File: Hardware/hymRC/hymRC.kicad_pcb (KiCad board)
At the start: 2 copper layers, 97.8 x 97.8 mm, 206 parts, among them J1 Relay_0, J10 EXT_AUD_IN, J11 EXT_AUD_OUT, J2 Digital Sensor Connector, J3 Analog Sensor Connector, J4 TX RADIO, J5 RX RADIO, J6 Relay_1, J7 Relay_2, J8 Relay_3, J9 Relay_4, K1 Role, K2 Role, K3 Role, K4 Role, K5 Role, Q1 BC817, Q2 NPN, Q3 NPN, Q4 NPN, Q5 NPN, U1 KT8870, U10 OptoCoupler, U11 OptoCoupler, U12 OptoCoupler, U13 OptoCoupler, U14 OptoCoupler, U2 MCP23017_SP, U3 OptoCoupler, U4 OptoCoupler, U5 OptoCoupler, U6 TL084, U7 TL084, U8 LM7808_TO220, U9 L7805, Y1 3.5795M

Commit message: Audio section completed
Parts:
- C10, C11, C12, C14, C15, C16, C17, C18, C19, C20, C21, C22, C23, C24, C25, C26, C27, C28, C29, C30, C31, C32, C33, C34, C35, C36, C37, C40, C41, C42, C43, C8, C9, R25, R26, R27, R28, R29, R30, R33, R34, R35, R36, R37, R38, R39, R42, R43, R48, R49, R50, R51, R52, R53, R54, R55, R56, R57, R58, R59, R60, R62, R63, R64, R65, U6, U7: moved to B.Cu
- moved C15 284.2 mm to (244.3, 79.2), turned to 90 degrees
- moved C37 283.8 mm to (237.5, 124.5)
- moved C16 279.9 mm to (233.0, 85.7), turned to 90 degrees
- moved C30 271.4 mm to (234.6, 108.3)
- moved C42 270.7 mm to (229.1, 124.6), turned to 180 degrees
- moved C41 269.6 mm to (229.1, 126.9)
- moved C13 269.1 mm to (219.7, 76.7), turned to 180 degrees
- moved C33 268.6 mm to (241.8, 111.5), turned to 90 degrees
- moved C36 267.4 mm to (224.7, 123.3), turned to 180 degrees
- moved C35 263.1 mm to (224.7, 129.4)
- moved C32 261.8 mm to (238.6, 112.6), turned to 180 degrees
- moved C34 259.2 mm to (237.4, 126.9), turned to 180 degrees
- moved C26 254.7 mm to (228.1, 108.3)
- moved C12 250.4 mm to (226.1, 85.1), turned to 90 degrees
- moved C43 246.8 mm to (229.1, 68.8), turned to 90 degrees
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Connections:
- C40 pad 1: Net-(C40-Pad1) -> GND
- C40 pad 2: Net-(C40-Pad2) -> Aku_12V
- C41 pad 1: Net-(C41-Pad1) -> GND
- C41 pad 2: Net-(C41-Pad2) -> Aku_12V
- C42 pad 1: Net-(C41-Pad2) -> Aku_12V
- C42 pad 2: Net-(C41-Pad1) -> GND
- C43 pad 1: Net-(C40-Pad2) -> Aku_12V
- C43 pad 2: Net-(C40-Pad1) -> GND
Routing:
- net Net-(C13-Pad2): track 0.00 -> 44.2 mm, vias 0 -> 2
- net /VCC_2: track 0.00 -> 42.6 mm, vias 0 -> 5
- net Net-(C12-Pad1): track 0.00 -> 22.8 mm, vias 0 -> 1
- net Net-(R33-Pad2): track 0.00 -> 20.7 mm
- net Aku_12V: track 0.00 -> 20.5 mm
- net Net-(C15-Pad2): track 0.00 -> 19.2 mm, vias 0 -> 1
- net Net-(R63-Pad2): track 0.00 -> 14.1 mm
- net Net-(C16-Pad2): track 0.00 -> 14.0 mm
- net Net-(C26-Pad2): track 0.00 -> 13.9 mm
- net Net-(R24-Pad2): track 0.00 -> 12.1 mm
- net Net-(C20-Pad1): track 0.00 -> 11.7 mm, vias 0 -> 1
- net Net-(R28-Pad2): track 0.00 -> 10.8 mm
- net Net-(C10-Pad2): track 0.00 -> 10.4 mm
- net GND: track 0.00 -> 9.86 mm
- net Net-(C8-Pad2): track 0.00 -> 9.29 mm, vias 0 -> 1
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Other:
- net class orta added: clearance 0.2, trace_width 0.5, via_dia 1, via_drill 0.5

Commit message: all connected somehow
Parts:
- added ?: , , F.Cu at (117.2, 120.6)
- added J12: 12V_AKU, TerminalBlock:TerminalBlock_bornier-2_P5.08mm, F.Cu at (116.3, 117.1)
- C38, D1, D2, Q1, Q2, Q5, R10, R100, R101, R102, R103, R104, R105, R106, R107, R11, R14, R15, R31, R4, R40, R44, R45, R46, R47, R5, R61, R66, R67, R68, R69, R70, R75, R76, R79, R8, R80, R81, R82, R83, R84, R85, R86, R87, R88, R9, R94, R95, R96, R97, R98, R99, U10, U11, U13, U14, U4, Y1: moved to B.Cu
- moved R72 281.7 mm to (-55.7, 193.0), turned to 180 degrees
- moved R71 263.3 mm to (-55.8, 189.7), turned to 180 degrees
- moved R73 237.2 mm to (-51.7, 186.1), turned to 90 degrees
- moved R74 228.3 mm to (-51.6, 197.0), turned to 90 degrees
- moved Y1 204.3 mm to (184.2, -64.5)
- moved R46 195.5 mm to (53.5, 80.6)
- moved C33 188.1 mm to (56.8, 77.5), turned to 180 degrees
- moved R58 185.4 mm to (55.6, 80.6), turned to 90 degrees
- moved RV5 183.8 mm to (57.4, 80.8), turned to 270 degrees
- moved C32 183.5 mm to (57.9, 80.6), turned to 270 degrees
- moved R59 183.3 mm to (61.0, 78.7), turned to 0 degrees
- moved C30 182.5 mm to (53.6, 84.7), turned to 90 degrees
- moved R57 180.7 mm to (55.8, 84.7), turned to 90 degrees
- moved C28 180.3 mm to (60.1, 81.9), turned to 270 degrees
- moved R61 180.0 mm to (69.7, 77.9), turned to 90 degrees
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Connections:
- J1 pad 1: R0_COM -> RO_NO
- J1 pad 2: R0_NC -> R0_COM
- J1 pad 3: RO_NO -> R0_NC
- J3 pad 1: /5V -> UART_RX
- J3 pad 2: Analog_Sensor1 -> UART_TX
- J3 pad 3: Analog_Sensor2 -> Analog_Sensor1
- J3 pad 4: Digital_IN0 -> Analog_Sensor2
- J3 pad 5: Digital_IN1 -> /5V
- J3 pad 7: UART_RX -> Digital_IN1
- J3 pad 8: UART_TX -> Digital_IN0
- J4 pad 1: /TX_AUDIO -> /TX_POWER
- J4 pad 2: GND -> /TX_PTT
- J4 pad 3: /TX_PTT -> /LINK_PTT_OUT
- J4 pad 4: /TX_POWER -> /TX_AUDIO
- J4 pad 5: /LINK_AUDIO_IN -> GND
- J4 pad 6: /LINK_PTT_OUT -> /LINK_AUDIO_IN
- J6 pad 1: R1_COM -> R1_NO
- J6 pad 2: R1_NC -> R1_COM
- J6 pad 3: R1_NO -> R1_NC
- J7 pad 1: R2_COM -> R2_NO
- J7 pad 2: R2_NC -> R2_COM
- J7 pad 3: R2_NO -> R2_NC
- J8 pad 1: R3_COM1 -> R3_NC1
- J8 pad 2: R3_NC1 -> R3_COM1
- J8 pad 4: R3_COM2 -> R3_NC2
- J8 pad 5: R3_NC2 -> R3_COM2
- J9 pad 1: R4_COM1 -> R4_NC1
- J9 pad 2: R4_NC1 -> R4_COM1
- J9 pad 4: R4_COM2 -> R4_NC2
- J9 pad 5: R4_NC2 -> R4_COM2
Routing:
- net R3_NC1: track 0.00 -> 42.9 mm
- net Aku_12V: track 20.5 -> 60.8 mm, vias 0 -> 1
- net /VIN: track 0.00 -> 39.1 mm
- net R3_COM1: track 0.00 -> 37.7 mm
- net Net-(C13-Pad2): track 44.2 -> 79.5 mm, vias 2 -> 4
- net GND: track 9.86 -> 42.1 mm
- net Net-(C24-Pad2): track 0.00 -> 30.7 mm, vias 0 -> 1
- net R3_NO1: track 0.00 -> 30.5 mm
- net R4_NC1: track 0.00 -> 23.6 mm
- net Net-(C34-Pad1): track 0.00 -> 22.2 mm, vias 0 -> 3
- net R3_NC2: track 0.00 -> 19.2 mm
- net R1_COM: track 0.00 -> 18.0 mm
- net /TX_POWER: track 0.00 -> 17.5 mm
- net Net-(C23-Pad2): track 0.00 -> 17.5 mm, vias 0 -> 1
- net R4_COM1: track 0.00 -> 17.4 mm
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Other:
- board text added: "---"

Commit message: digitals connected
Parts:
- C44, C45, R18, R19, R71, R72, R73, R74, U5: moved to B.Cu
- R81, R82, R83, R84, U10: moved to F.Cu
- moved C2 175.2 mm to (91.4, 74.6), turned to 180 degrees
- moved C46 174.9 mm to (95.6, 74.7)
- moved R3 172.6 mm to (90.4, 71.6), turned to 90 degrees
- moved R18 171.3 mm to (65.1, 70.3), turned to 90 degrees
- moved R19 170.5 mm to (63.0, 70.4), turned to 90 degrees
- moved U2 165.4 mm to (70.0, 70.2)
- moved C47 165.4 mm to (92.3, 64.4), turned to 180 degrees
- moved U1 161.1 mm to (96.8, 69.5), turned to 180 degrees
- moved R1 159.2 mm to (105.1, 71.3), turned to 270 degrees
- moved R2 158.2 mm to (103.0, 71.0), turned to 270 degrees
- moved C1 156.0 mm to (107.3, 71.3)
- moved C45 155.6 mm to (68.5, 70.2), turned to 270 degrees
- moved Y1 154.3 mm to (104.4, 67.6), turned to 270 degrees
- moved C44 150.1 mm to (70.7, 70.2), turned to 90 degrees
- moved R72 149.8 mm to (71.9, 114.6), turned to 0 degrees
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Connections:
- J5 pad 1: /RX_AUDIO -> /RX_SQL
- J5 pad 2: GND -> /LINK_SQL
- J5 pad 4: /RX_SQL -> /RX_AUDIO
- J5 pad 5: /LINK_SQL -> GND
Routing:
- net /LINK_SQUELCH: track 0.00 -> 149.7 mm, vias 0 -> 2
- net /SQUELCH: track 0.00 -> 146.5 mm, vias 0 -> 1
- net /PTT_CTRL: track 0.00 -> 114.1 mm, vias 0 -> 1
- net UART_RX: track 0.00 -> 42.8 mm
- net UART_TX: track 0.00 -> 38.8 mm
- net Net-(C36-Pad2): track 9.56 -> 33.4 mm
- net /Q4: track 0.00 -> 21.0 mm
- net /Q3: track 0.00 -> 19.5 mm
- net /Q2: track 0.00 -> 17.9 mm
- net /Q1: track 0.00 -> 15.8 mm
- net /LINK_SQL: track 0.00 -> 13.7 mm
- net Net-(R71-Pad1): track 0.00 -> 11.8 mm
- net Net-(R82-Pad1): track 0.00 -> 10.6 mm
- net /VCC_2: track 53.6 -> 44.0 mm
- net /5V: track 11.9 -> 21.2 mm, vias 0 -> 1
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
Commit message: routing finished
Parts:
- moved R44 2.99 mm to (47.5, 50.3), turned to 0 degrees
- moved C39 2.50 mm to (48.5, 69.2)
- moved R102 2.13 mm to (55.0, 64.0), turned to 0 degrees
- moved J4 1.94 mm to (34.0, 122.8)
- moved C47 1.84 mm to (90.4, 64.4)
- moved J5 1.73 mm to (65.3, 122.8)
- moved R104 1.17 mm to (31.4, 107.8), turned to 90 degrees
- moved J10 0.64 mm to (84.2, 114.3)
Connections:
- A1 pad 25: /TX_PWR_CTRL -> /LINK_PTT_CTRL
- A1 pad 26: /LINK_PTT_CTRL -> /TX_PWR_CTRL
- J2 pad 2: SPI_SS -> SPI_MISO
- J2 pad 4: SPI_MISO -> SPI_SS
- J2 pad 6: Digital_Sensor_CS1 -> Digital_Sensor_CS3
- J2 pad 8: Digital_Sensor_CS3 -> Digital_Sensor_CS1
- J5 pad 3: /LINK_AUDIO_OUT -> /RX_AUDIO
- J5 pad 4: /RX_AUDIO -> /LINK_AUDIO_OUT
- R16 pad 2: /CONTROL_OUTPUT_2 -> /CONTROL_OUTPUT_0
- R4 pad 2: /CONTROL_OUTPUT_0 -> /CONTROL_OUTPUT_2
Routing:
- net /5V: track 21.2 -> 376.7 mm, vias 1 -> 9
- net Aku_12V: track 63.0 -> 384.6 mm, vias 1 -> 7
- net /TX_PWR_CTRL: track 0.00 -> 180.7 mm, vias 0 -> 3
- net /LINK_PTT_CTRL: track 0.00 -> 171.7 mm, vias 0 -> 3
- net /CONTROL_OUTPUT_3: track 0.00 -> 108.1 mm, vias 0 -> 4
- net SPI_MISO: track 0.00 -> 103.0 mm
- net SPI_MOSI: track 0.00 -> 100.4 mm
- net SPI_SS: track 0.00 -> 97.4 mm
- net DTMF_In: track 0.00 -> 93.2 mm, vias 0 -> 5
- net /Analog0: track 2.18 -> 93.1 mm, vias 0 -> 1
- net /TX_AUDIO: track 0.00 -> 87.7 mm, vias 0 -> 3
- net /LINK_AUDIO_IN: track 0.00 -> 85.9 mm, vias 0 -> 1
- net /INTA: track 0.00 -> 78.2 mm, vias 0 -> 2
- net SPI_SCK: track 0.00 -> 77.2 mm
- net /VIN: track 39.1 -> 115.3 mm
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- added copper zone on B.Cu, net GND
- added copper zone on F.Cu, net GND

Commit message: 3d finished
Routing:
- net GND: track 69.8 -> 105.9 mm, vias 131 -> 153
- net /CONTROL_INPUT_1: track 46.4 -> 45.7 mm
- net (no net): vias 8 -> 3

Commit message: all done
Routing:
- net Net-(C13-Pad2): track 93.2 -> 94.3 mm
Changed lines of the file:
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@@
   (general
     (thickness 1.6)
-    (drawings 24)
-    (tracks 1650)
+    (drawings 38)
+    (tracks 1652)
     (zones 0)
     (modules 208)
@@
     (44 Edge.Cuts user)
     (45 Margin user)
-    (46 B.CrtYd user)
-    (47 F.CrtYd user)
+    (46 B.CrtYd user hide)
+    (47 F.CrtYd user hide)
     (48 B.Fab user hide)
     (49 F.Fab user hide)
@@
       (net 72 "Net-(C36-Pad2)"))
     (model ${KISYS3DMOD}/TerminalBlock.3dshapes/TerminalBlock_bornier-2_P5.08mm.wrl
-      (offset (xyz 2.539999961853027 0 0))
+      (offset (xyz 2.54 0 0))
       (scale (xyz 1 1 1))
-      (rotate (xyz 0 0 0))
+      (rotate (xyz 0 0 -95))
+    )
+    (model ${KIPRJMOD}/3D/TerminalBlock_1x02_P3.50mm_Horizontal.wrl
+      (offset (xyz 5 0 0))
+      (scale (xyz 1 0.7 0.7))
+      (rotate (xyz 0 0 -180))
     )
   )
@@
     )
   )
+  (gr_poly (pts (xy 30.734 37.211) (xy 28.194 39.243) (xy 22.86 39.243) (xy 22.86 31.75) (xy 30.734 31.75)) (layer F.Mask) (width 0.1))
+  (gr_poly (pts (xy 115.189 39.624) (xy 113.157 37.084) (xy 113.157 31.75) (xy 120.65 31.75) (xy 120.65 39.624)) (layer F.Mask) (width 0.1))
+  (gr_poly (pts (xy 112.776 124.079) (xy 115.316 122.047) (xy 120.65 122.047) (xy 120.65 129.54) (xy 112.776 129.54)) (layer F.Mask) (width 0.1))
+  (gr_poly (pts (xy 28.321 121.666) (xy 30.353 124.206) (xy 30.353 129.54) (xy 22.86 129.54) (xy 22.86 121.666)) (layer F.Mask) (width 0.1))
+  (gr_poly (pts (xy 102.235 107.442) (xy 100.711 107.442) (xy 100.711 80.899) (xy 102.235 80.899)) (layer B.Mask) (width 0.1))
+  (gr_poly (pts (xy 101.854 107.442) (xy 73.787 107.442) (xy 73.787 105.918) (xy 101.854 105.918)) (layer B.Mask) (width 0.1))
+  (gr_poly (pts (xy 101.6 82.423) (xy 73.533 82.423) (xy 73.533 80.899) (xy 101.6 80.899)) (layer B.Mask) (width 0.1))
+  (gr_poly (pts (xy 73.787 104.775) (xy 72.263 104.775) (xy 72.263 102.489) (xy 73.787 102.489)) (layer B.Mask) (width 0.1))
+  (gr_poly (pts (xy 73.787 101.6) (xy 72.263 101.6) (xy 72.263 88.011) (xy 73.787 88.011)) (layer B.Mask) (width 0.1))
+  (gr_poly (pts (xy 73.787 109.347) (xy 72.263 109.347) (xy 72.263 105.918) (xy 73.787 105.918)) (layer B.Mask) (width 0.1))
+  (gr_poly (pts (xy 73.787 86.614) (xy 72.263 86.614) (xy 72.263 78.105) (xy 73.787 78.105)) (layer B.Mask) (width 0.1))
+  (gr_poly (pts (xy 47.244 109.347) (xy 45.72 109.347) (xy 45.72 78.105) (xy 47.244 78.105)) (layer B.Mask) (width 0.1))
+  (gr_poly (pts (xy 73.787 109.982) (xy 45.72 109.982) (xy 45.72 108.458) (xy 73.787 108.458)) (layer B.Mask) (width 0.1))
+  (gr_poly (pts (xy 73.787 78.994) (xy 45.72 78.994) (xy 45.72 77.47) (xy 73.787 77.47)) (layer B.Mask) (width 0.1))
   (gr_line (start 46.482 108.9025) (end 46.482 108.2675) (layer Dwgs.User) (width 0.15))
   (gr_line (start 73.2155 108.9025) (end 46.482 108.9025) (layer Dwgs.User) (width 0.15))
@@
   (segment (start 105.791 111.878) (end 103.3455 111.878) (width 1) (layer F.Cu) (net 35))
   (via (at 74.676 102.108) (size 0.8) (drill 0.4) (layers F.Cu B.Cu) (net 35))
-  (segment (start 74.676 102.108) (end 72.39 102.108) (width 0.25) (layer B.Cu) (net 35))
-  (segment (start 72.39 102.108) (end 72.39 104.013) (width 0.25) (layer B.Cu) (net 35))
-  (segment (start 64.378499 104.684999) (end 64.262 104.5685) (width 0.25) (layer B.Cu) (net 35))
-  (segment (start 71.718001 104.684999) (end 64.378499 104.684999) (width 0.25) (layer B.Cu) (net 35))
-  (segment (start 72.39 104.013) (end 71.718001 104.684999) (width 0.25) (layer B.Cu) (net 35))
   (segment (start 77.597 102.108) (end 74.676 102.108) (width 0.25) (layer F.Cu) (net 35))
   (segment (start 79.375 100.33) (end 77.597 102.108) (width 0.25) (layer F.Cu) (net 35))
@@
   (segment (start 74.549 102.235) (end 74.676 102.108) (width 0.25) (layer B.Cu) (net 35))
   (segment (start 74.549 104.394) (end 74.549 102.235) (width 0.25) (layer B.Cu) (net 35))
+  (segment (start 64.378499 104.684999) (end 64.262 104.5685) (width 0.25) (layer B.Cu) (net 35))
+  (segment (start 71.755 104.013) (end 71.083001 104.684999) (width 0.25) (layer B.Cu) (net 35))
+  (segment (start 71.755 102.362) (end 71.755 104.013) (width 0.25) (layer B.Cu) (net 35))
+  (segment (start 72.009 102.108) (end 71.755 102.362) (width 0.25) (layer B.Cu) (net 35))
+  (segment (start 71.083001 104.684999) (end 64.378499 104.684999) (width 0.25) (layer B.Cu) (net 35))
+  (segment (start 74.676 102.108) (end 72.009 102.108) (width 0.25) (layer B.Cu) (net 35))
   (segment (start 65.786 96.2765) (end 65.786 97.8535) (width 0.25) (layer F.Cu) (net 36))
   (segment (start 65.786 97.8535) (end 66.548 98.6155) (width 0.25) (layer F.Cu) (net 36))
@@
   (segment (start 96.4565 94.602) (end 98.5415 96.687) (width 0.25) (layer F.Cu) (net 43))
   (segment (start 96.4565 85.471) (end 96.4565 94.602) (width 0.25) (layer F.Cu) (net 43))
-  (segment (start 73.4695 87.503) (end 78.6765 87.503) (width 0.25) (layer B.Cu) (net 43))
-  (segment (start 71.247 89.7255) (end 73.4695 87.503) (width 0.25) (layer B.Cu) (net 43))
+  (segment (start 71.628 87.503) (end 78.6765 87.503) (width 0.25) (layer B.Cu) (net 43))
+  (segment (start 71.247 87.884) (end 71.628 87.503) (width 0.25) (layer B.Cu) (net 43))
+  (segment (start 71.247 89.7255) (end 71.247 87.884) (width 0.25) (layer B.Cu) (net 43))
   (segment (start 54.5045 103.955) (end 54.626 104.0765) (width 0.25) (layer B.Cu) (net 44))
   (segment (start 54.5045 102.0445) (end 54.5045 103.955) (width 0.25) (layer B.Cu) (net 44))

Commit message: Titles added
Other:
- board text added: "Designed by TA7W/OH2UDS - Baris DINC - 2021 V1.01"
- board text added: "TNX to TA7OM Huda for support"
- board text added: "hymRC Repeater Controller"

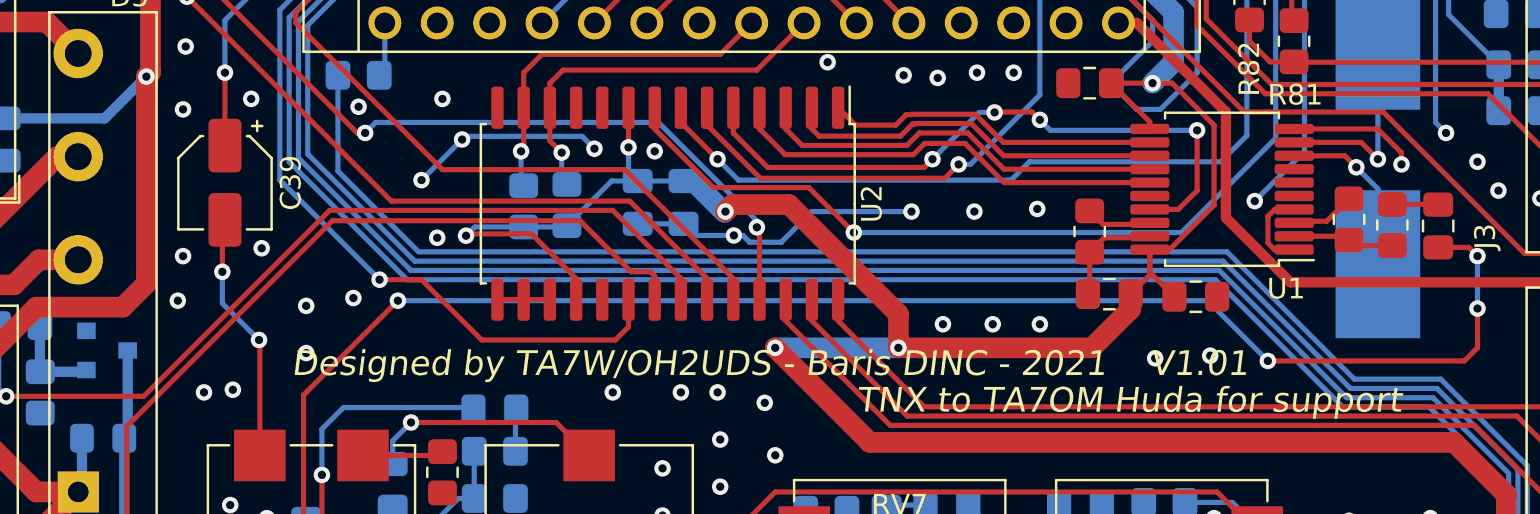
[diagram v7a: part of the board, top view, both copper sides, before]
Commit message: SOIC-20 footprint squeezed
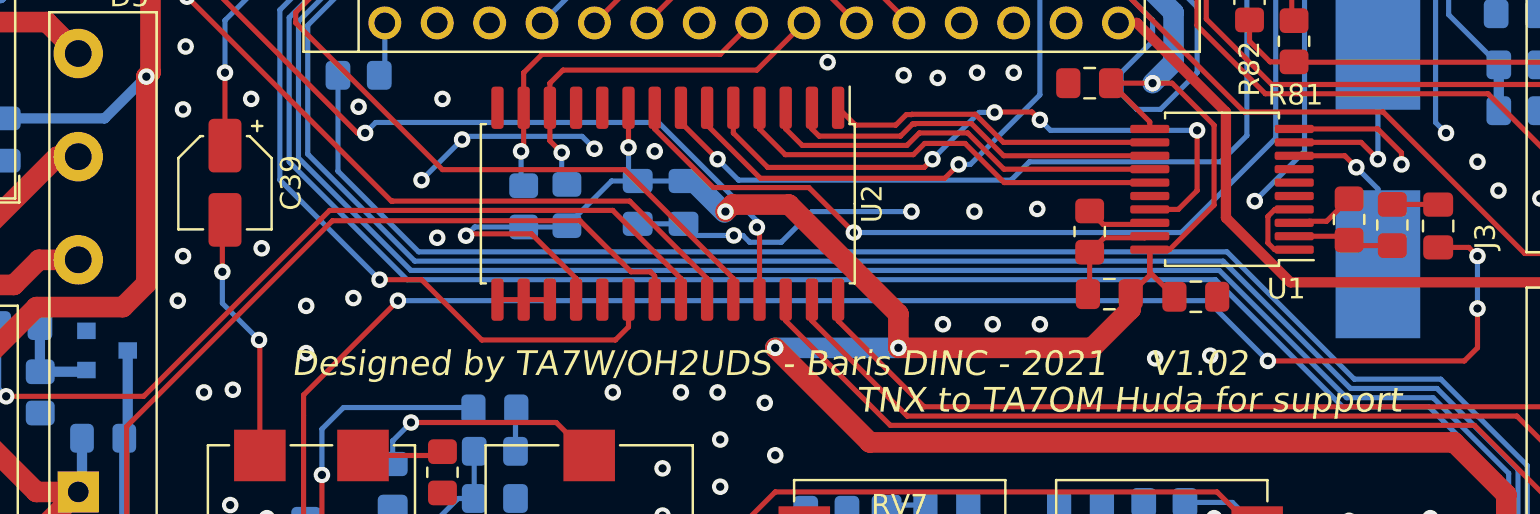
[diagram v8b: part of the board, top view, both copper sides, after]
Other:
- board text added: "Designed by TA7W/OH2UDS - Baris DINC - 2021 V1.02"
- board text removed: "Designed by TA7W/OH2UDS - Baris DINC - 2021 V1.01"
